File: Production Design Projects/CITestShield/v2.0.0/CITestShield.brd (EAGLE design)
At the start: 53.3 x 54.6 mm, 36 parts, among them CON1 MICRO-SD, IC4 LM75BD, SW1 SPST-4_TP1154_J

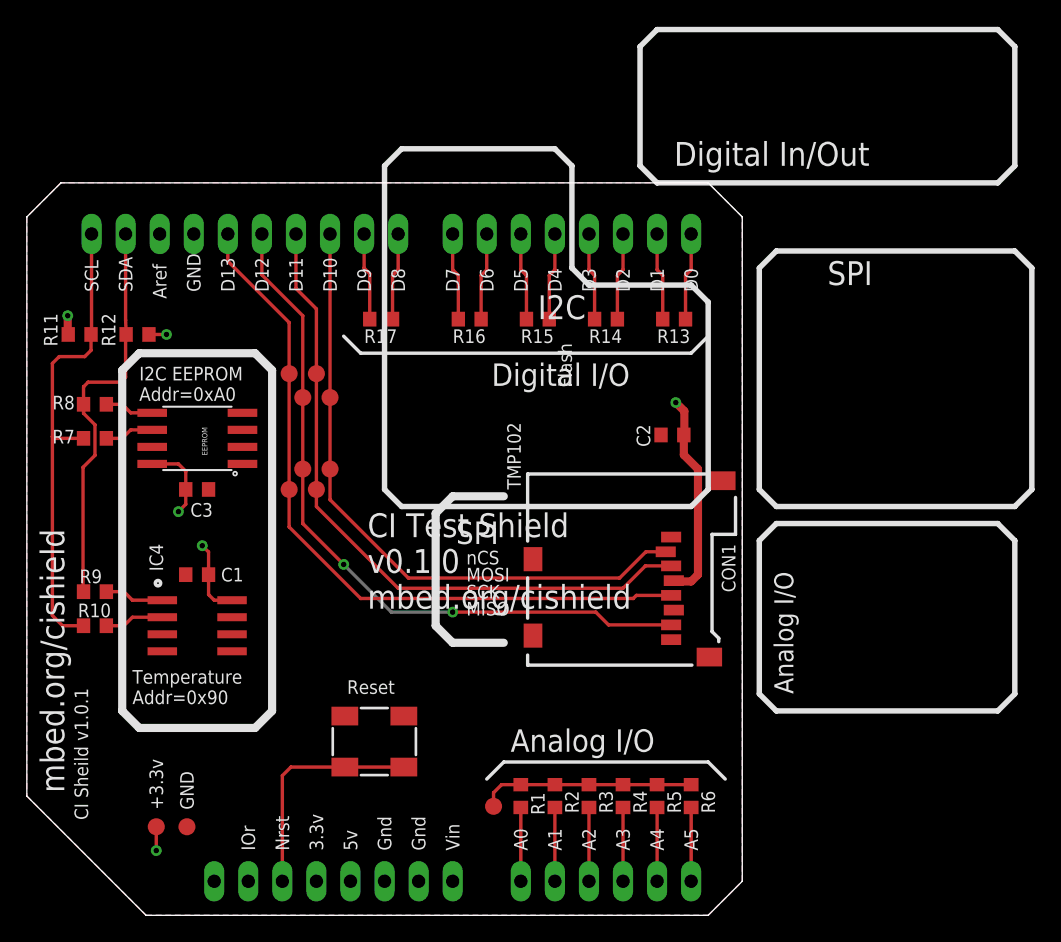
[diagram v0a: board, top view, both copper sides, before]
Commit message: Release of v2.0.0 CI test shield, removal of R13(UART Tests Removed)
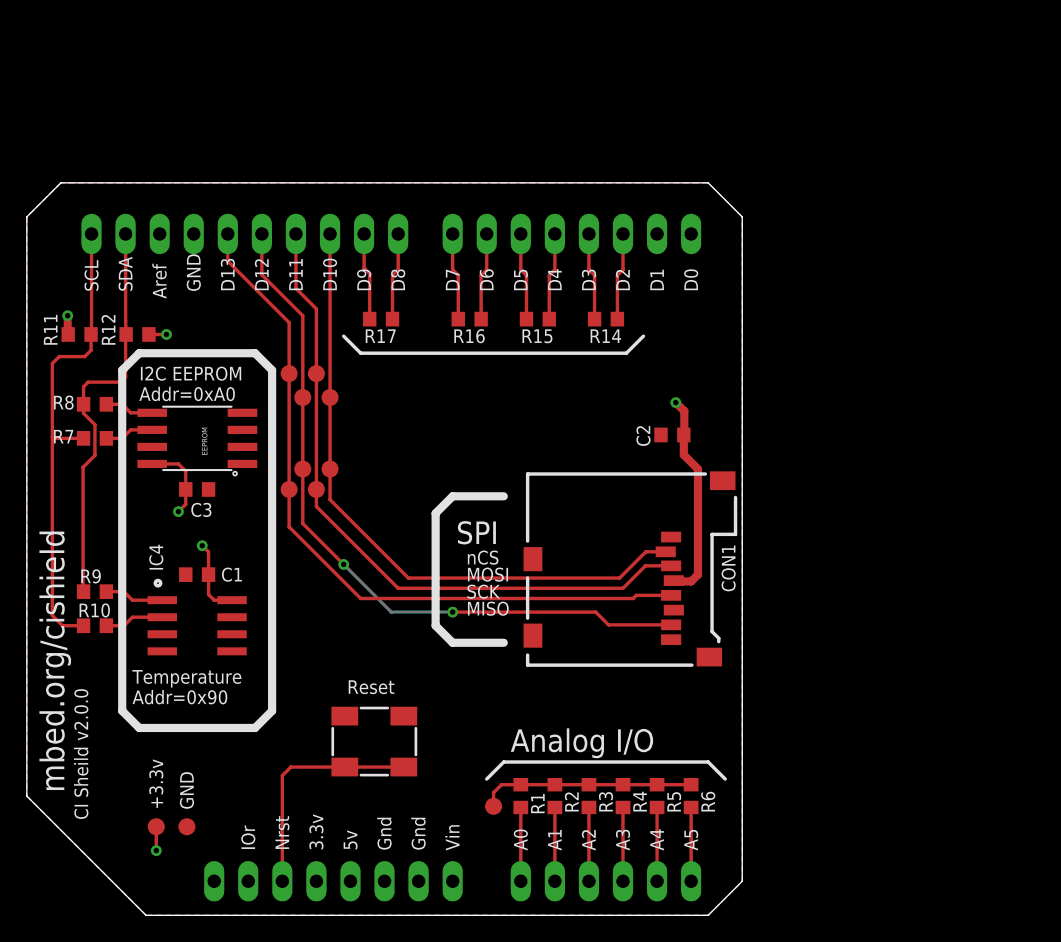
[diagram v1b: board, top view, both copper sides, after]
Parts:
- removed R13: 0R, mbed-HDK:0603
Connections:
- removed net N$12: BRD1.16, R13.2
- removed net N$13: BRD1.15, R13.1
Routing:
- net N$13: track 6.52 -> 0.00 mm
- net N$12: track 6.52 -> 0.00 mm
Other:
- board text added: "CI Sheild v2.0.0"
- board text added: "SPI - microSD Write/Read"
- board text removed: "CI Sheild v1.0.1"
- board text removed: "CI Test Shield v0.1.0 mbed.org/cishield"
- board text removed: "Digital I/O"
- board text removed: "Digital In/Out"
- board text removed: "Flash"
- board text removed: "I2C"
- board text removed: "SPIP - microSD Write/Read"
- board text removed: "TMP102"
- board text removed: "Tests Analog I/O - A0-5 mesh Digital I/O - D0-D9 loopback UART - D0/1 loopback SPI - micoSD W/R I2C - Flash / Temp Sensor PWM - Loopback Interrupt In - Loopback"
- board text removed: "UART - D0/1 loopback"
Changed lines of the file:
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@@
 <?xml version="1.0" encoding="utf-8"?>
 <!DOCTYPE eagle SYSTEM "eagle.dtd">
-<eagle version="7.3.0">
+<eagle version="7.6.0">
 <drawing>
 <settings>
@@
 <setting verticaltext="up"/>
 </settings>
-<grid distance="0.01" unitdist="inch" unit="inch" style="lines" multiple="1" display="yes" altdistance="0.025" altunitdist="inch" altunit="inch"/>
+<grid distance="0.1" unitdist="inch" unit="inch" style="lines" multiple="1" display="yes" altdistance="0.025" altunitdist="inch" altunit="inch"/>
 <layers>
 <layer number="1" name="Top" color="4" fill="1" visible="yes" active="yes"/>
@@
 <layer number="20" name="Dimension" color="15" fill="1" visible="yes" active="yes"/>
 <layer number="21" name="tPlace" color="7" fill="1" visible="yes" active="yes"/>
-<layer number="22" name="bPlace" color="7" fill="1" visible="no" active="yes"/>
+<layer number="22" name="bPlace" color="7" fill="1" visible="yes" active="yes"/>
 <layer number="23" name="tOrigins" color="15" fill="1" visible="yes" active="yes"/>
 <layer number="24" name="bOrigins" color="15" fill="1" visible="no" active="yes"/>
@@
 <board>
 <plain>
-<text x="73.66" y="46.99" size="1.778" layer="121" font="vector">SPI</text>
-<text x="52.07" y="44.45" size="1.778" layer="121" font="vector">I2C</text>
-<text x="71.12" y="16.51" size="1.4224" layer="121" font="vector" rot="R90">Analog I/O</text>
-<text x="62.23" y="55.88" size="1.778" layer="121" font="vector">Digital In/Out</text>
-<text x="39.37" y="22.86" size="1.778" layer="121" font="vector">CI Test Shield
-v0.1.0
-mbed.org/cishield</text>
-<text x="87.63" y="41.91" size="1.778" layer="122" font="vector" rot="MR0">Tests
-Analog I/O - A0-5 mesh
-Digital I/O - D0-D9 loopback
-UART - D0/1 loopback
-SPI - micoSD W/R
-I2C - Flash / Temp Sensor
-PWM - Loopback
-Interrupt In - Loopback</text>
-<text x="50.8" y="31.75" size="1.016" layer="121" rot="R90">TMP102</text>
-<text x="54.61" y="39.37" size="1.016" layer="121" font="vector" rot="R90">Flash</text>
-<wire x1="69.85" y1="29.21" x2="86.36" y2="29.21" width="0.4064" layer="121"/>
-<wire x1="86.36" y1="29.21" x2="87.63" y2="27.94" width="0.4064" layer="121"/>
-<wire x1="87.63" y1="27.94" x2="87.63" y2="16.51" width="0.4064" layer="121"/>
-<wire x1="87.63" y1="16.51" x2="86.36" y2="15.24" width="0.4064" layer="121"/>
-<wire x1="86.36" y1="15.24" x2="69.85" y2="15.24" width="0.4064" layer="121"/>
-<wire x1="69.85" y1="15.24" x2="68.58" y2="16.51" width="0.4064" layer="121"/>
-<wire x1="68.58" y1="16.51" x2="68.58" y2="27.94" width="0.4064" layer="121"/>
-<wire x1="68.58" y1="27.94" x2="69.85" y2="29.21" width="0.4064" layer="121"/>
-<wire x1="60.96" y1="66.04" x2="86.36" y2="66.04" width="0.4064" layer="121"/>
-<wire x1="86.36" y1="66.04" x2="87.63" y2="64.77" width="0.4064" layer="121"/>
-<wire x1="87.63" y1="64.77" x2="87.63" y2="55.88" width="0.4064" layer="121"/>
-<wire x1="87.63" y1="55.88" x2="86.36" y2="54.61" width="0.4064" layer="121"/>
-<wire x1="86.36" y1="54.61" x2="60.96" y2="54.61" width="0.4064" layer="121"/>
-<wire x1="60.96" y1="54.61" x2="59.69" y2="55.88" width="0.4064" layer="121"/>
-<wire x1="59.69" y1="55.88" x2="59.69" y2="64.77" width="0.4064" layer="121"/>
-<wire x1="59.69" y1="64.77" x2="60.96" y2="66.04" width="0.4064" layer="121"/>
-<wire x1="87.63" y1="30.48" x2="69.85" y2="30.48" width="0.4064" layer="121"/>
-<wire x1="69.85" y1="30.48" x2="68.58" y2="31.75" width="0.4064" layer="121"/>
-<wire x1="68.58" y1="31.75" x2="68.58" y2="48.26" width="0.4064" layer="121"/>
-<wire x1="68.58" y1="48.26" x2="69.85" y2="49.53" width="0.4064" layer="121"/>
-<wire x1="69.85" y1="49.53" x2="87.63" y2="49.53" width="0.4064" layer="121"/>
-<wire x1="87.63" y1="49.53" x2="88.9" y2="48.26" width="0.4064" layer="121"/>
-<wire x1="88.9" y1="48.26" x2="88.9" y2="31.75" width="0.4064" layer="121"/>
-<wire x1="88.9" y1="31.75" x2="87.63" y2="30.48" width="0.4064" layer="121"/>
-<wire x1="41.91" y1="57.15" x2="53.34" y2="57.15" width="0.4064" layer="121"/>
-<wire x1="53.34" y1="57.15" x2="54.61" y2="55.88" width="0.4064" layer="121"/>
-<wire x1="54.61" y1="55.88" x2="54.61" y2="48.26" width="0.4064" layer="121"/>
-<wire x1="54.61" y1="48.26" x2="55.88" y2="46.99" width="0.4064" layer="121"/>
-<wire x1="55.88" y1="46.99" x2="63.5" y2="46.99" width="0.4064" layer="121"/>
-<wire x1="63.5" y1="46.99" x2="64.77" y2="45.72" width="0.4064" layer="121"/>
-<wire x1="64.77" y1="45.72" x2="64.77" y2="31.75" width="0.4064" layer="121"/>
-<wire x1="64.77" y1="31.75" x2="63.5" y2="30.48" width="0.4064" layer="121"/>
-<wire x1="63.5" y1="30.48" x2="41.91" y2="30.48" width="0.4064" layer="121"/>
-<wire x1="41.91" y1="30.48" x2="40.64" y2="31.75" width="0.4064" layer="121"/>
-<wire x1="40.64" y1="31.75" x2="40.64" y2="55.88" width="0.4064" layer="121"/>
-<wire x1="40.64" y1="55.88" x2="41.91" y2="57.15" width="0.4064" layer="121"/>
 <wire x1="13.97" y1="8.89" x2="22.86" y2="0" width="0" layer="20"/>
 <wire x1="22.86" y1="0" x2="64.77" y2="0" width="0" layer="20"/>
@@
 <text x="30.988" y="4.826" size="1.016" layer="21" font="vector" ratio="12" rot="R90">IOr</text>
 <wire x1="37.592" y1="43.18" x2="38.862" y2="41.91" width="0.254" layer="21"/>
-<wire x1="38.862" y1="41.91" x2="63.5" y2="41.91" width="0.254" layer="21"/>
-<wire x1="63.5" y1="41.91" x2="64.77" y2="43.18" width="0.254" layer="21"/>
+<wire x1="38.862" y1="41.91" x2="58.674" y2="41.91" width="0.254" layer="21"/>
+<wire x1="58.674" y1="41.91" x2="59.944" y2="43.18" width="0.254" layer="21"/>
 <wire x1="48.26" y1="10.16" x2="49.53" y2="11.43" width="0.254" layer="21"/>
 <wire x1="49.53" y1="11.43" x2="64.77" y2="11.43" width="0.254" layer="21"/>
 <wire x1="64.77" y1="11.43" x2="66.04" y2="10.16" width="0.254" layer="21"/>
 <text x="50.038" y="12.192" size="1.6764" layer="21" font="vector" ratio="12">Analog I/O</text>
-<text x="58.928" y="41.148" size="1.6764" layer="21" font="vector" ratio="12" rot="R180">Digital I/O</text>
 <text x="45.974" y="27.686" size="1.6764" layer="21" font="vector" ratio="12">SPI</text>
 <text x="46.736" y="26.162" size="1.016" layer="21" font="vector" ratio="12">nCS</text>
@@
 <text x="22.352" y="38.354" size="1.016" layer="21" font="vector" ratio="12">Addr=0xA0</text>
 <text x="21.844" y="15.748" size="1.016" layer="21" font="vector" ratio="12">Addr=0x90</text>
-<text x="18.542" y="7.112" size="1.016" layer="21" ratio="12" rot="R90">CI Sheild v1.0.1</text>
+<text x="18.542" y="7.112" size="1.016" layer="21" ratio="12" rot="R90">CI Sheild v2.0.0</text>
 <text x="60.96" y="43.18" size="1.6764" layer="22" ratio="12" rot="MR0">Tests :</text>
 <text x="58.42" y="40.64" size="1.016" layer="22" ratio="12" rot="MR0">Analog I/O - A0-5 mesh</text>
 <text x="58.42" y="38.1" size="1.016" layer="22" ratio="12" rot="MR0">Digital I/O - D0-9 loopback</text>
-<text x="58.42" y="35.56" size="1.016" layer="22" ratio="12" rot="MR0">UART - D0/1 loopback</text>
-<text x="58.42" y="33.02" size="1.016" layer="22" ratio="12" rot="MR0">SPIP - microSD Write/Read</text>
-<text x="58.42" y="30.48" size="1.016" layer="22" ratio="12" rot="MR0">I2C - Flash / Temp sensor</text>
-<text x="58.42" y="27.94" size="1.016" layer="22" ratio="12" rot="MR0">PWM - Loopback</text>
-<text x="58.42" y="25.4" size="1.016" layer="22" ratio="12" rot="MR0">Interrupt In - Loopback</text>
+<text x="58.42" y="35.56" size="1.016" layer="22" ratio="12" rot="MR0"></text>
+<text x="58.42" y="35.56" size="1.016" layer="22" ratio="12" rot="MR0">SPI - microSD Write/Read</text>
+<text x="58.42" y="33.02" size="1.016" layer="22" ratio="12" rot="MR0">I2C - Flash / Temp sensor</text>
+<text x="58.42" y="30.48" size="1.016" layer="22" ratio="12" rot="MR0">PWM - Loopback</text>
+<text x="58.42" y="27.94" size="1.016" layer="22" ratio="12" rot="MR0">Interrupt In - Loopback</text>
 <wire x1="22.352" y1="41.91" x2="21.082" y2="40.64" width="0.6096" layer="21"/>
 <wire x1="21.082" y1="40.64" x2="21.082" y2="15.24" width="0.6096" layer="21"/>
@@
 <attribute name="VALUE" x="33.782" y="18.542" size="1.016" layer="27" font="vector" ratio="12" rot="R90"/>
 </element>
-<element name="R13" library="mbed-HDK" package="0603" value="0R" x="62.23" y="44.45" locked="yes" smashed="yes" rot="R180">
-<attribute name="NAME" x="60.96" y="42.672" size="1.016" layer="25" font="vector" ratio="12"/>
-<attribute name="VALUE" x="63.246" y="40.386" size="1.016" layer="27" font="vector" ratio="12" rot="R90"/>
-</element>
 <element name="R14" library="mbed-HDK" package="0603" value="0R" x="57.15" y="44.45" locked="yes" smashed="yes" rot="R180">
 <attribute name="NAME" x="55.88" y="42.672" size="1.016" layer="25" font="vector" ratio="12"/>
@@
 <wire x1="41.656" y1="48.133" x2="41.656" y2="50.8" width="0.254" layer="1"/>
 </signal>
-<signal name="N$12">
-<contactref element="BRD1" pad="16"/>
-<contactref element="R13" pad="2"/>
-<wire x1="61.38" y1="44.45" x2="61.38" y2="47.713" width="0.254" layer="1"/>
-<wire x1="61.38" y1="47.713" x2="60.96" y2="48.133" width="0.254" layer="1"/>
-<wire x1="60.96" y1="48.133" x2="60.96" y2="50.8" width="0.254" layer="1"/>
-</signal>
-<signal name="N$13">
-<contactref element="BRD1" pad="15"/>
-<contactref element="R13" pad="1"/>
-<wire x1="63.08" y1="44.45" x2="63.08" y2="47.713" width="0.254" layer="1"/>
-<wire x1="63.08" y1="47.713" x2="63.5" y2="48.133" width="0.254" layer="1"/>
-<wire x1="63.5" y1="48.133" x2="63.5" y2="50.8" width="0.254" layer="1"/>
-</signal>
 <signal name="N$14">
 <contactref element="BRD1" pad="17"/>
@@
 </board>
 </drawing>
-<compatibility>
-<note version="6.3" minversion="6.2.2" severity="warning">
-Since Version 6.2.2 text objects can contain more than one line,
-which will not be processed correctly with this version.
-</note>
-</compatibility>
 </eagle>
